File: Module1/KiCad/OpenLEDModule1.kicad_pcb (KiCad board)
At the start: 2 copper layers, 29.2 x 29.2 mm, 10 parts, among them P1 CONN2, P2 CONN1

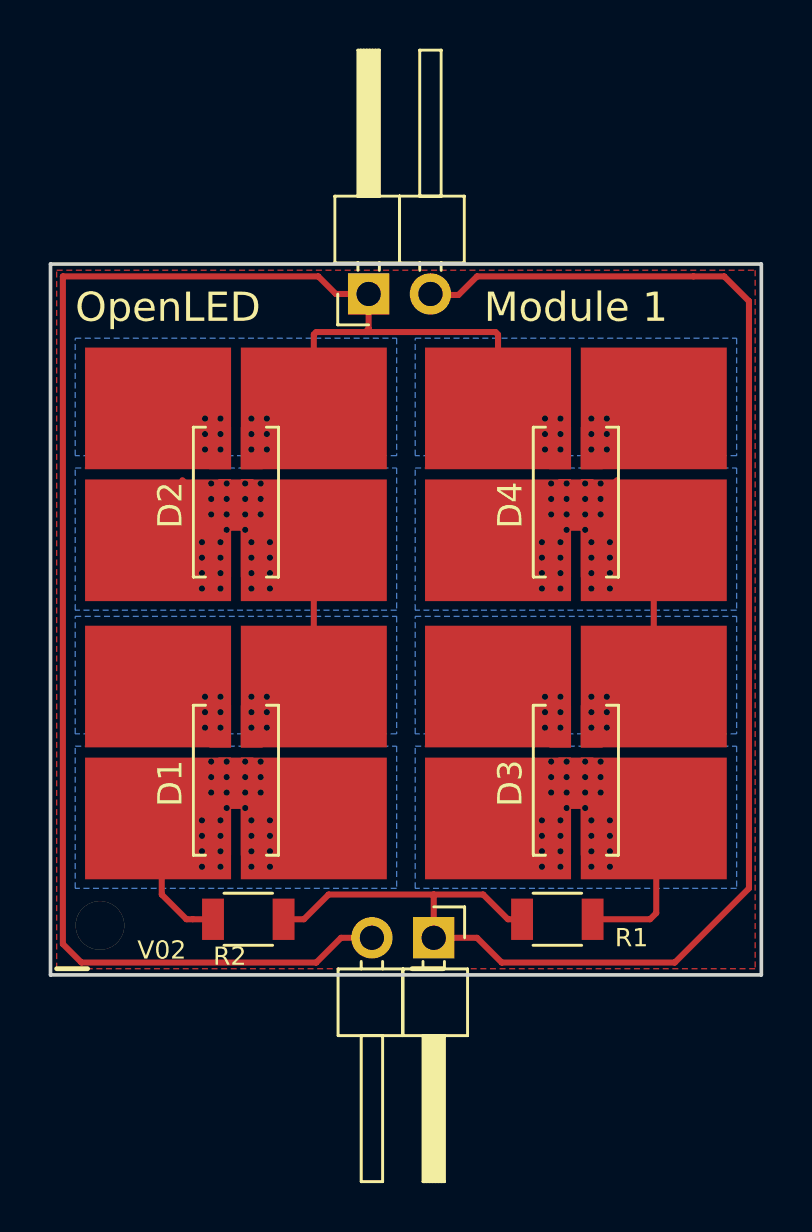
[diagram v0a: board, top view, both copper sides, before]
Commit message: Fixed issues #1 (header supports), #3 (four holes), #4 (polarity text). Added enhancment #8 (LED orientation marker)
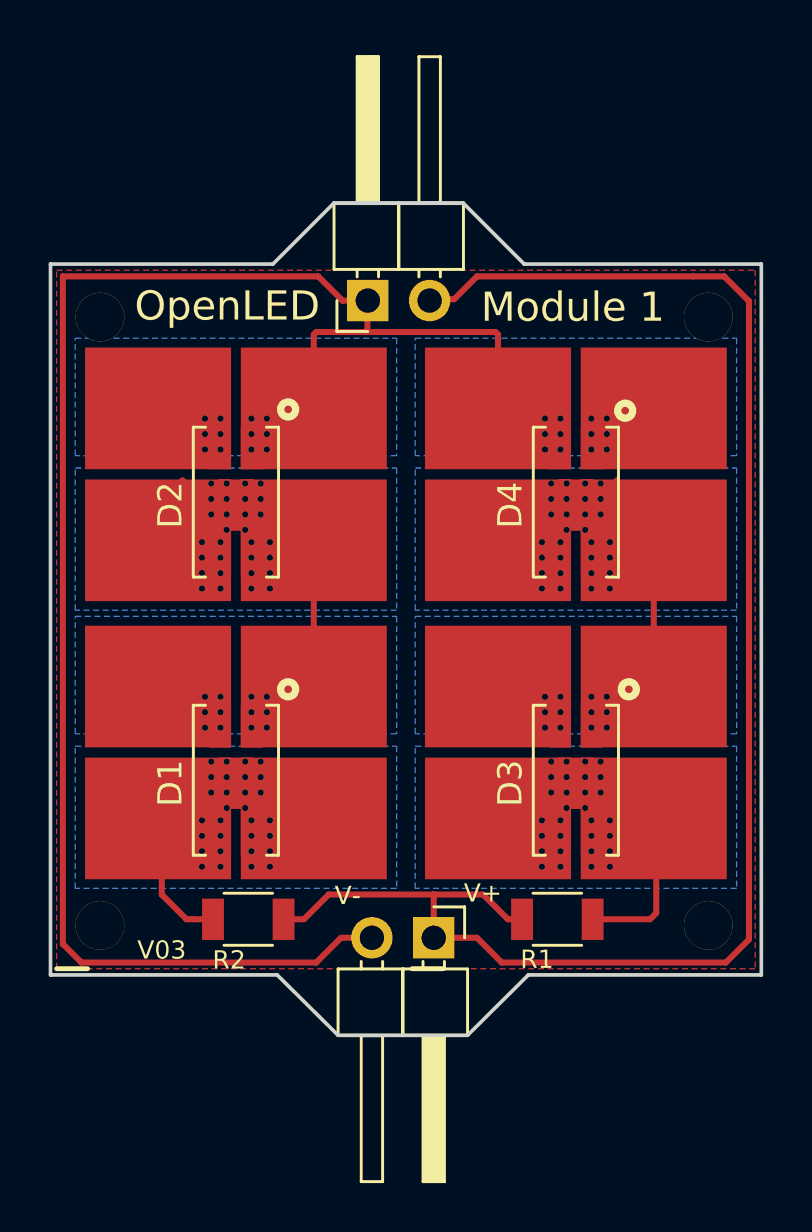
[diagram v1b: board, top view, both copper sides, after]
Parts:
- added ?: , OpenLed:DRILLHOLE, F.Cu at (138.9, 72.3)
- added ?: , OpenLed:DRILLHOLE, F.Cu at (163.9, 72.3)
- added ?: , OpenLed:DRILLHOLE, F.Cu at (163.9, 97.3)
- added QRCODE: LOGO, OpenLed:qrcode_olm_inverse2, B.Cu at (151.8, 83.2)
- moved P1 0.27 mm to (150.2, 71.3)
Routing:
- net +24V: track 65.0 -> 66.4 mm
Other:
- board size 29.2 x 29.2 mm -> 29.2 x 34.2 mm
- board text added: "V+"
- board text added: "V-"
- board text added: "V03"
- board text added: "www.openledmodule.info"
- board text removed: "V02"
